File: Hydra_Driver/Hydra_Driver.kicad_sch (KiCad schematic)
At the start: 43 parts, among them IC1 ESP32-S3-WROOM-1-N4, J1 USB4105-GF-A, J10 Conn_01x03, J11 Conn_01x04, J12 Conn_01x03, J13 Conn_01x02, J2 Conn_01x02, J3 Conn_01x06, J4 Conn_01x03, J5 Conn_01x04, J6 Conn_01x03, J7 Conn_01x02, J8 Conn_01x03, J9 Conn_01x06, SW1 SW_SPST, SW2 SW_SPST, U1 USBLC6-2SC6, U2 MIC5504-3.3YM5-TR

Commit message: Finished routing for Hydra V2
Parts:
- removed C11, C9: 0.1u, Capacitor_SMD:C_0402_1005Metric, symbol Device:C_Small
- removed J10, J4, J8: Conn_01x03, Connector_PinSocket_2.54mm:PinSocket_1x03_P2.54mm_Vertical, symbol Connector_Generic:Conn_01x03
- removed J7: Conn_01x02, Connector_PinHeader_2.54mm:PinHeader_1x02_P2.54mm_Vertical, symbol Connector_Generic:Conn_01x02
- removed R8: 10k, Resistor_SMD:R_0402_1005Metric, symbol Device:R
- added C109, C111, C113: 0.1u, Capacitor_SMD:C_0402_1005Metric, symbol Device:C_Small
- added U103: SN74LVC1G373DCKR, Touchstone:SOT65P210X110-6N, symbol SN74LVC1G373DCKR:SN74LVC1G373DCKR
- J102: renamed from J2; footprint TerminalBlock:TerminalBlock_MaiXu_MX126-5.0-02P_1x02_P5.00mm -> Touchstone:AMASS_XT30U-F_1x02_P5.0mm_Vertical
- J104: renamed from J5; footprint Connector_PinHeader_2.54mm:PinHeader_1x04_P2.54mm_Horizontal -> Touchstone:CONN_CCSH-W10R-04TR-BK-A_ADA
- J105: renamed from J6; footprint Connector_PinHeader_2.54mm:PinHeader_1x03_P2.54mm_Horizontal -> Connector_JST:JST_XH_S3B-XH-A-1_1x03_P2.50mm_Horizontal
- J107: renamed from J11; footprint Connector_PinHeader_2.54mm:PinHeader_1x04_P2.54mm_Horizontal -> Touchstone:CONN_CCSH-W10R-04TR-BK-A_ADA
- J108: renamed from J12; footprint Connector_PinHeader_2.54mm:PinHeader_1x03_P2.54mm_Horizontal -> Connector_JST:JST_XH_S3B-XH-A-1_1x03_P2.50mm_Horizontal
- J109: renamed from J13; footprint TerminalBlock:TerminalBlock_MaiXu_MX126-5.0-02P_1x02_P5.00mm -> Touchstone:AMASS_XT30U-F_1x02_P5.0mm_Vertical
- SW101: renamed from SW1; footprint Button_Switch_THT:SW_PUSH_6mm -> Touchstone:SW_B3U-1000P
- SW102: renamed from SW2; footprint Button_Switch_THT:SW_PUSH_6mm -> Touchstone:SW_B3U-1000P
- renumbered C1 to C101, C2 to C102, C3 to C103, C4 to C104, C5 to C105, C6 to C106, C7 to C107, C8 to C108, C10 to C110, C12 to C112, D1 to D101, D2 to D102, D3 to D103, IC1 to IC101, J1 to J101, J3 to J103, J9 to J106, R1 to R101, R2 to R102, R3 to R103, R4 to R104, R5 to R105, R6 to R106, R7 to R107, R9 to R108, R10 to R109, U1 to U101, U2 to U102
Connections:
- net LOOP1 is gone; now on net CLK: J103.3 (Pin_3)
- net LOOP2 is gone; now on net CLK: J106.3 (Pin_3)
- net +3.3V: now also C111.1, C113.1, U103.5 (VCC)
- net +5V: now also C109.1
- net CLK: no longer J103.2 (Pin_2), J106.2 (Pin_2)
- net GND: now also C109.2, C111.2, C113.2, U103.2 (GND), U103.6 (~{OE})
- net IN1A: now also IC101.12 (IO8); no longer IC101.11 (IO18)
- net OUT1A: now also J105.3 (Pin_3); no longer J105.1 (Pin_1)
- net OUT1B: now also J108.3 (Pin_3); no longer J108.1 (Pin_1)
- net OUT3A: now also J105.1 (Pin_1); no longer J105.3 (Pin_3)
- net OUT3B: now also J108.1 (Pin_1); no longer J108.3 (Pin_3)
- net SENSE1A: now also IC101.11 (IO18); no longer IC101.10 (IO17)
- net SENSE2A: now also IC101.10 (IO17); no longer IC101.9 (IO16)
- net SENSE3B: now reaches IC101.5 (IO5)
- net CS renamed CSCK
- net CSCK: now also U103.1 (LE); no longer IC101.8 (IO15)
- new net CSIN: IC101.8 (IO15), J103.2 (Pin_2), U103.3 (D)
- new net CSOUT: J106.2 (Pin_2), U103.4 (Q)
- new net SENSE3A: IC101.9 (IO16)
- no-connect marks 7 -> 6
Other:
- sheet Driver_Unit ports: added SENSE3; removed none
- sheet Driver_Unit1 ports: added SENSE3; removed none
- moved on the sheet: C108, C112, J105, J108, U102

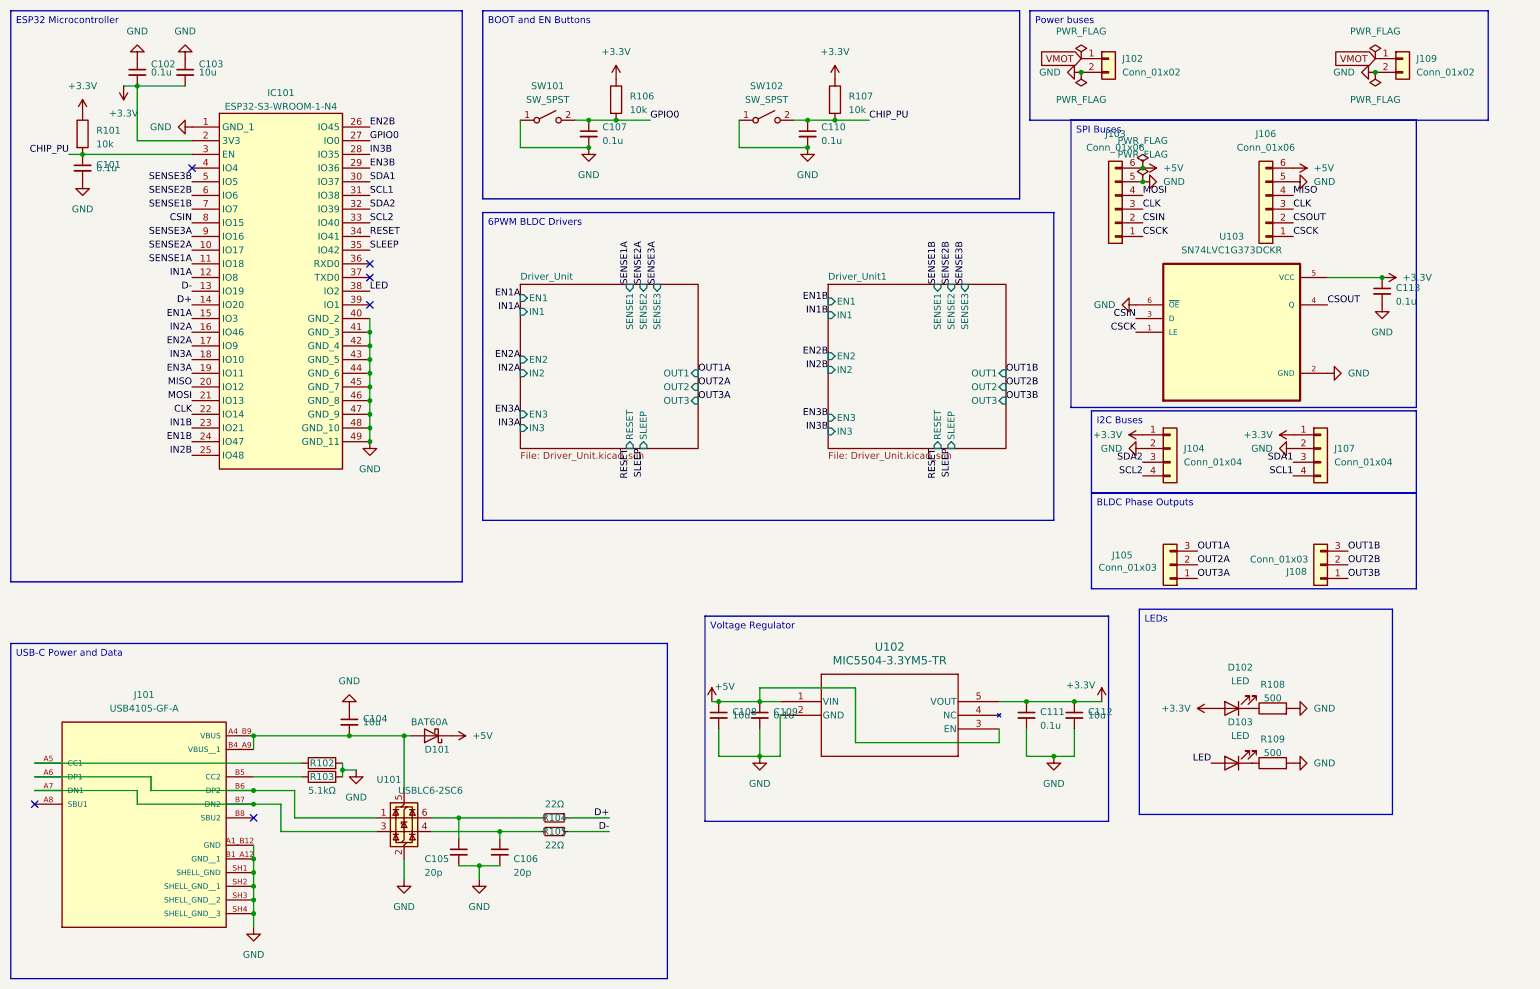
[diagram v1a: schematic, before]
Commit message: Used correct flip flop for CS sequencing, added pullup
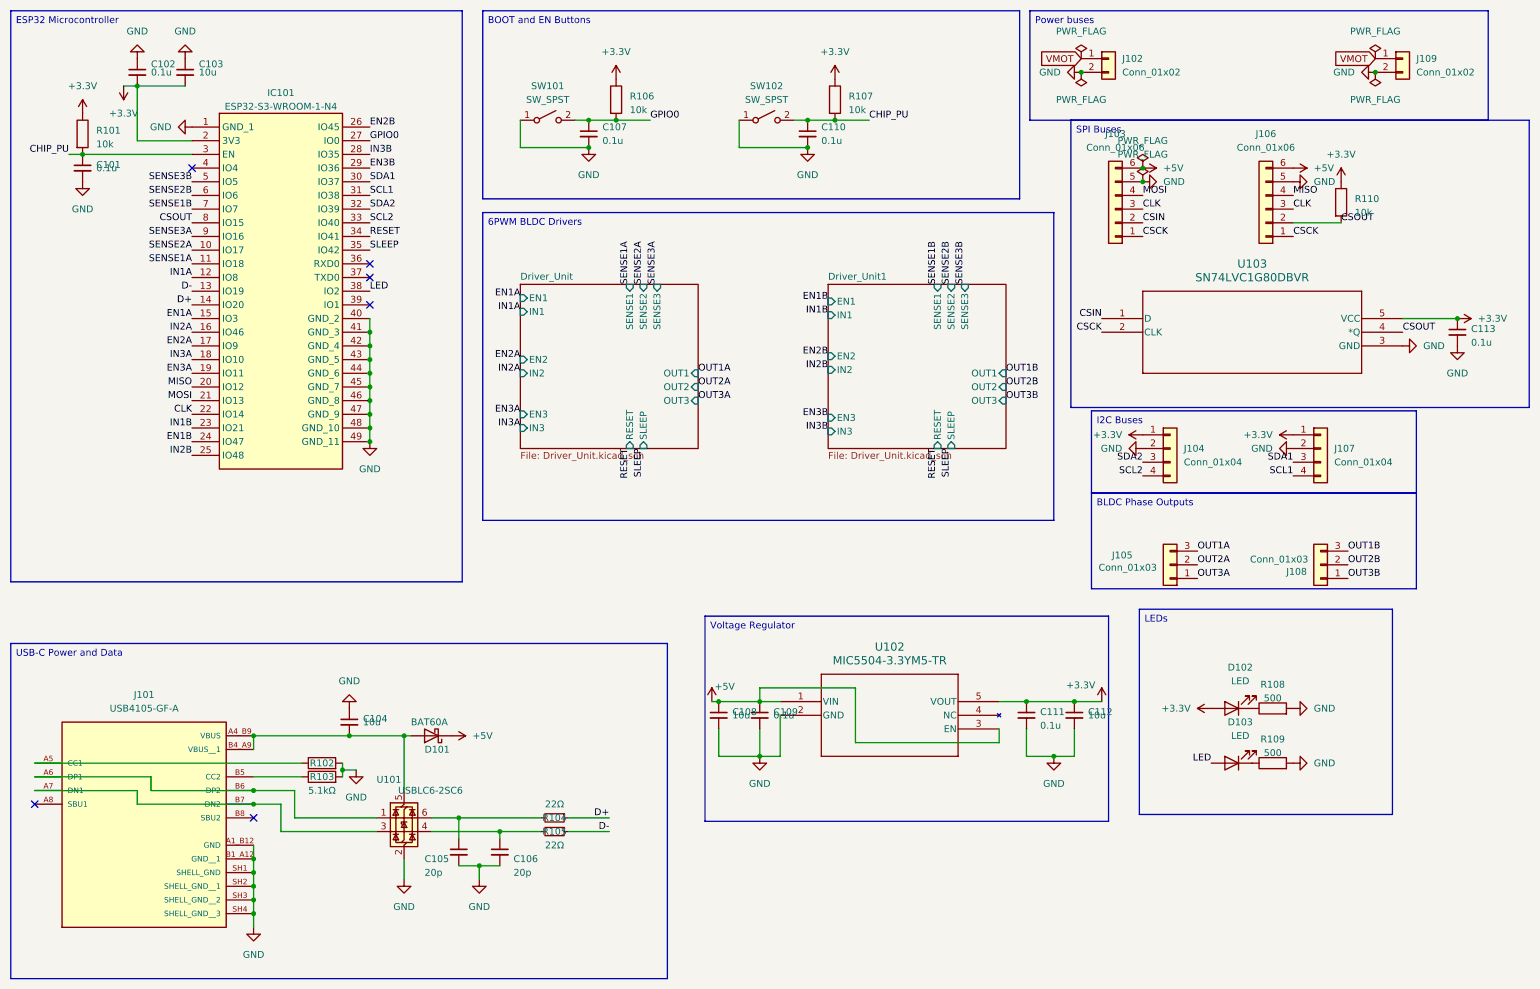
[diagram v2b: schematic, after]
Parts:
- removed U103: SN74LVC1G373DCKR, Touchstone:SOT65P210X110-6N, symbol SN74LVC1G373DCKR:SN74LVC1G373DCKR
- added R110: 10k, Resistor_SMD:R_0402_1005Metric, symbol Device:R
- added U103: SN74LVC1G80DBVR, Touchstone:DBV5, symbol SN74LVC1G80DBVR:SN74LVC1G80DBVR
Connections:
- net +3.3V: now also R110.1, U103.5 (VCC)
- net CSCK: now also U103.2 (CLK)
- net CSIN: now also U103.1 (D); no longer IC101.8 (IO15)
- net CSOUT: now also IC101.8 (IO15), R110.2, U103.4 (*Q)
- net GND: now also U103.3 (GND)
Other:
- moved on the sheet: C113
